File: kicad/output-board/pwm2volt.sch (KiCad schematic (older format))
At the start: 22 parts, among them U11 LM324

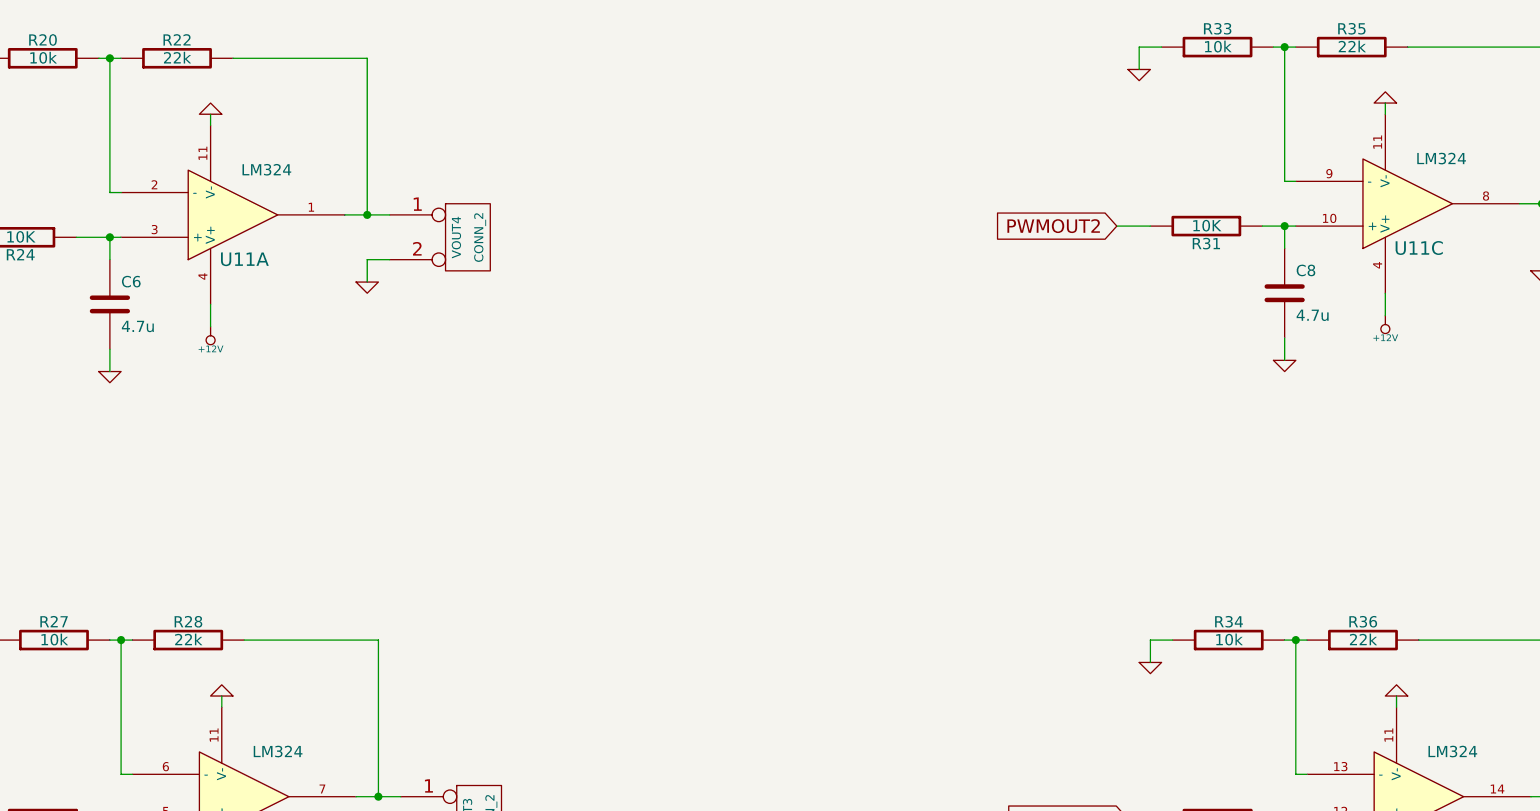
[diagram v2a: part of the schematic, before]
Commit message: Lowered OP-amp gain
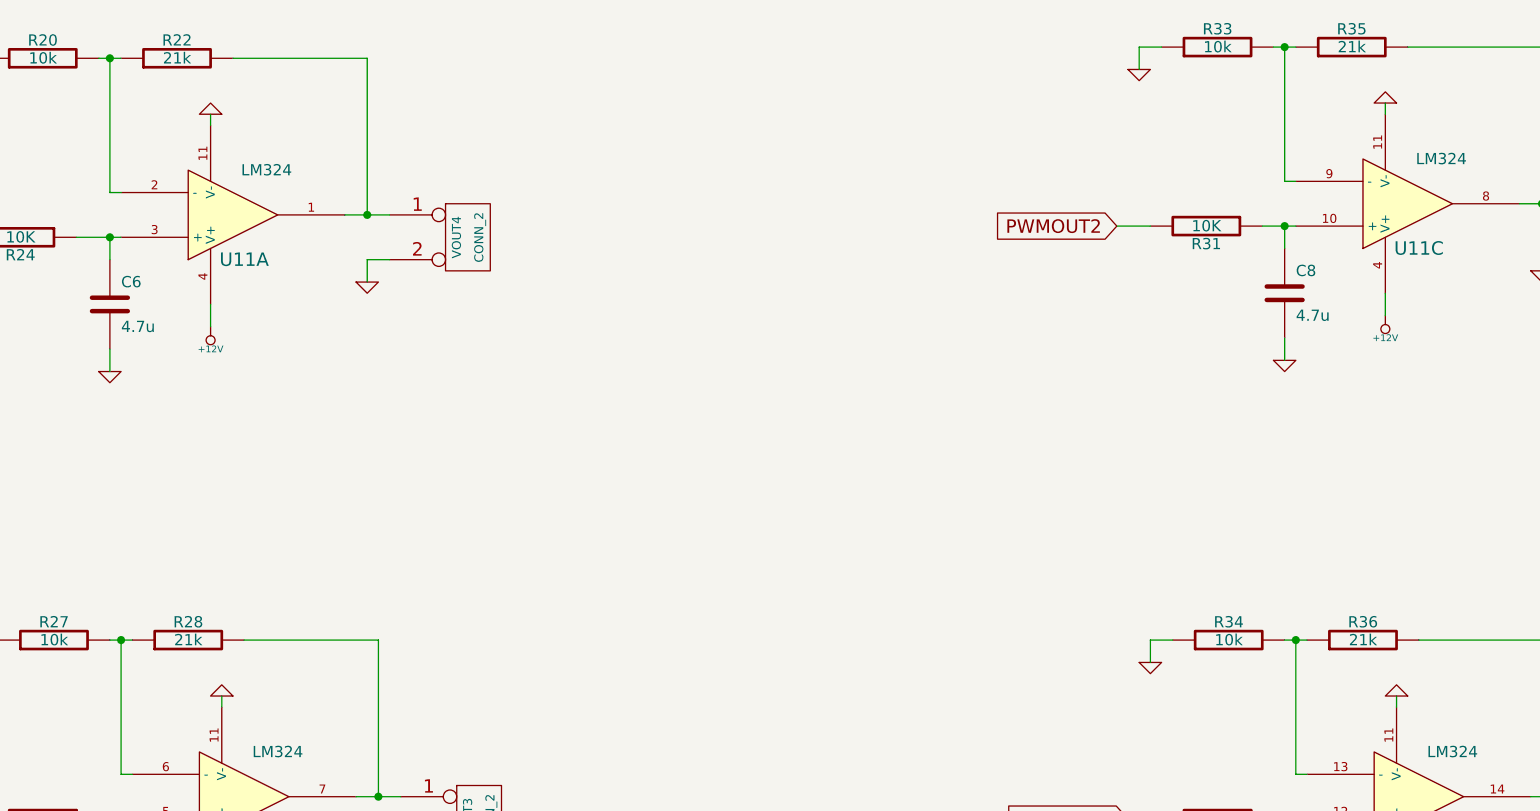
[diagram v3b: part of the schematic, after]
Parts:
- R22, R28, R35, R36: value 22k -> 21k
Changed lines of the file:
@@
-EESchema Schematic File Version 2  date Mon 06 Aug 2012 06:14:15 PM CEST
+EESchema Schematic File Version 2  date Sat 18 Aug 2012 05:22:02 PM CEST
 LIBS:power
 LIBS:device
@@
 LIBS:toshiba
 LIBS:output-board-cache
-EELAYER 25  0
+EELAYER 24  0
 EELAYER END
 $Descr A4 11700 8267
 Sheet 2 3
 Title "panStamp relay and 0-10V output board"
-Date "6 aug 2012"
+Date "18 aug 2012"
 Rev "1.2"
 Comp "www.panstamp.com"
@@
 P 9050 1200
 F 0 "R35" V 9130 1200 50  0000 C CNN
-F 1 "22k" V 9050 1200 50  0000 C CNN
+F 1 "21k" V 9050 1200 50  0000 C CNN
 F 2 "SM0603S" H 9050 1200 60  0001 C CNN
 	1    9050 1200
@@
 P 9100 3850
 F 0 "R36" V 9180 3850 50  0000 C CNN
-F 1 "22k" V 9100 3850 50  0000 C CNN
+F 1 "21k" V 9100 3850 50  0000 C CNN
 F 2 "SM0603S" H 9100 3850 60  0001 C CNN
 	1    9100 3850
@@
 P 3850 3850
 F 0 "R28" V 3930 3850 50  0000 C CNN
-F 1 "22k" V 3850 3850 50  0000 C CNN
+F 1 "21k" V 3850 3850 50  0000 C CNN
 F 2 "SM0603S" H 3850 3850 60  0001 C CNN
 	1    3850 3850
@@
 P 3800 1250
 F 0 "R22" V 3880 1250 50  0000 C CNN
-F 1 "22k" V 3800 1250 50  0000 C CNN
+F 1 "21k" V 3800 1250 50  0000 C CNN
 F 2 "SM0603S" H 3800 1250 60  0001 C CNN
 	1    3800 1250
